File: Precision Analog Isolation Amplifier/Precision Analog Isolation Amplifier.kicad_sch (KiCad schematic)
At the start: 20 parts, among them J1 Conn_Coaxial, J2 Conn_Coaxial, Q1 2N3906, U1 HCNR201, U2 TLV172IDCK, U3 TLV172IDCK

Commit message: Add few components & Start PCB design
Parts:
- added C1, C13, C5, C9: 47u, Capacitor_SMD:C_0805_2012Metric_Pad1.18x1.45mm_HandSolder, symbol Device:C
- added C11, C12, C15, C16, C3, C4, C7, C8: C, Capacitor_SMD:C_0805_2012Metric_Pad1.18x1.45mm_HandSolder, symbol Device:C
- added FB1, FB2, FB3, FB4: FerriteBead_Small, Inductor_SMD:L_1206_3216Metric, symbol Device:FerriteBead_Small
- added J1, J2: Conn_01x03, Connector_PinHeader_2.54mm:PinHeader_1x03_P2.54mm_Vertical, symbol Connector_Generic:Conn_01x03
- C10: renamed from C4; footprint (none) -> Capacitor_SMD:C_0805_2012Metric_Pad1.18x1.45mm_HandSolder
- C14: renamed from C6; footprint (none) -> Capacitor_SMD:C_0805_2012Metric_Pad1.18x1.45mm_HandSolder
- C17: renamed from C2; footprint (none) -> Capacitor_SMD:C_0805_2012Metric_Pad1.18x1.45mm_HandSolder
- C18: renamed from C5; value C -> 33p; footprint (none) -> Capacitor_SMD:C_0805_2012Metric_Pad1.18x1.45mm_HandSolder
- C2: renamed from C1; footprint (none) -> Capacitor_SMD:C_0805_2012Metric_Pad1.18x1.45mm_HandSolder
- C6: renamed from C3; footprint (none) -> Capacitor_SMD:C_0805_2012Metric_Pad1.18x1.45mm_HandSolder
- J3: renamed from J1; footprint (none) -> Connector_Coaxial:SMA_Amphenol_132289_EdgeMount
- J4: renamed from J2; footprint (none) -> Connector_Coaxial:SMA_Amphenol_132289_EdgeMount
- R1, R2, R3, R6: footprint (none) -> Resistor_SMD:R_0805_2012Metric_Pad1.20x1.40mm_HandSolder
- R4: renamed from R5; footprint (none) -> Resistor_SMD:R_0805_2012Metric_Pad1.20x1.40mm_HandSolder
- R5: renamed from R4; footprint (none) -> Resistor_SMD:R_0805_2012Metric_Pad1.20x1.40mm_HandSolder
- RV1: footprint (none) -> Potentiometer_THT:Potentiometer_Bourns_3386W_Horizontal
- U2, U3: footprint Package_TO_SOT_SMD:SOT-353_SC-70-5 -> (none)
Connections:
- net GND1: now also C1.1, C3.1, C4.1, C5.1, C7.1, C8.1, J1.2 (Pin_2)
- net GND2: now also C11.1, C12.1, C13.1, C15.1, C16.1, C9.1, J2.2 (Pin_2)
- net VCC1 +15V: now also FB1.1, J1.1 (Pin_1); no longer C2.2
- net VCC2 +15V: now also FB3.1, J2.1 (Pin_1); no longer C10.2
- net VEE1 -15V: now also FB2.1, J1.3 (Pin_3); no longer C6.2
- net VEE2 -15V: now also FB4.1, J2.3 (Pin_3); no longer C14.2
- new net: C1.2, C2.2, C3.2, C4.2, FB1.2
- new net: C13.2, C14.2, C15.2, C16.2, FB4.2
- new net: C5.2, C6.2, C7.2, C8.2, FB2.2
- new net: C10.2, C11.2, C12.2, C9.2, FB3.2
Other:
- moved on the sheet: C10, C14, C17, C18, C2, C6, D1, J3, J4, Q1, R1, R2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

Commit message: Update Schematic & PCB
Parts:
- removed U2, U3: TLV172IDCK, symbol Amplifier_Operational:TLV172IDCK
- added C19, C20: 0.1uF, Capacitor_SMD:C_0805_2012Metric_Pad1.18x1.45mm_HandSolder, symbol Device:C
- added IC1: ADA4899-1YRDZ, SOIC127P600X175-9N, symbol ADA4899:ADA4899-1YRDZ
- added R7: 50R, Resistor_SMD:R_0805_2012Metric_Pad1.20x1.40mm_HandSolder, symbol Device:R
- added U2, U4: ADA4522, ADA4522:SOIC127P600X175-8N, symbol Amplifier_Operational:OPA1692xDGK
- D1: value 1N4150 -> ---; footprint (none) -> Diode_SMD:D_0805_2012Metric_Pad1.15x1.40mm_HandSolder
- Q1: value 2N3906 -> ---; footprint (none) -> Package_TO_SOT_SMD:SOT-23_Handsoldering
- U1: footprint (none) -> HCNR201-300E:HCNR201300E
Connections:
- net GND1: now also U4.3 (+)
- net GND2: now also C19.1, C20.1, IC1.9 (EP), U2.3 (+)
- net VCC1 +15V: now also C1.2, C2.2, C3.2, C4.2, FB1.2, U4.8 (V+); no longer FB1.1, J1.1 (Pin_1)
- net VCC2 +15V: now also C10.2, C11.2, C12.2, C9.2, FB3.2, C20.2, IC1.7 (+VS), U2.8 (V+); no longer FB3.1, J2.1 (Pin_1)
- net VEE1 -15V: now also C5.2, C6.2, C7.2, C8.2, FB2.2, U4.4 (V-); no longer FB2.1, J1.3 (Pin_3)
- net VEE2 -15V: now also C13.2, C14.2, C15.2, C16.2, FB4.2, C19.2, IC1.4 (-VS_1), U2.4 (V-); no longer FB4.1, J2.3 (Pin_3)
- net at C17.1, R4.2, U1.3 (K): now also U4.2 (-)
- net at C17.2, R3.2: now also U4.1
- net at C18.2, R6.1, U1.6 (K): now also U2.2 (-)
- net Vsep_out: now reaches C18.1, RV1.1, RV1.2
- net Vsep_out: now also R7.1, U2.1; no longer J4.1 (In)
- new net: IC1.3 (+IN), R7.2
- new net VCC1 IN +15V: FB1.1, J1.1 (Pin_1)
- new net VCC2 IN +15V: FB3.1, J2.1 (Pin_1)
- new net VEE1 IN -15V: FB2.1, J1.3 (Pin_3)
- new net VEE2 IN -15V: FB4.1, J2.3 (Pin_3)
- new net Vout: IC1.2 (-IN), IC1.6 (VOUT), J4.1 (In)
- no-connect marks 0 -> 9
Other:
- note added: "Część pierwotna"
- note added: "Część wtórna"
- note added: "NC"
- note added: "Wtórnik napięciowy"
- note added: "Zasilanie"
- moved on the sheet: C1, C10, C11, C12, C13, C14, C15, C16, C17, C18, C2, C3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

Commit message: Update PCB
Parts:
- added D2, D3, D4, D5: SMAJ15A, Diode_SMD:D_SMA, symbol Diode:SMAJ15A
- added D6, D7, D8, D9: LED, Diode_SMD:D_0805_2012Metric_Pad1.15x1.40mm_HandSolder, symbol Device:LED
- added F1, F2, F3, F4: Fuse, Resistor_SMD:R_0805_2012Metric_Pad1.20x1.40mm_HandSolder, symbol Device:Fuse
- added R10, R11, R8, R9: 33k, Resistor_SMD:R_0805_2012Metric_Pad1.20x1.40mm_HandSolder, symbol Device:R
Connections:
- net GND1: now also D2.1 (A1), D3.2 (A2), R8.2, R9.2
- net GND2: now also D4.1 (A1), D5.2 (A2), R10.2, R11.2
- net VCC1 +15V: now also D6.2 (A)
- net VCC1 IN +15V: now also D3.1 (A1), F2.1; no longer J1.1 (Pin_1)
- net VCC2 +15V: now also D9.2 (A)
- net VCC2 IN +15V: now also D5.1 (A1), F3.1; no longer J2.1 (Pin_1)
- net VEE1 -15V: now also D7.1 (K)
- net VEE1 IN -15V: now also D2.2 (A2), F1.1; no longer J1.3 (Pin_3)
- net VEE2 -15V: now also D8.1 (K)
- net VEE2 IN -15V: now also D4.2 (A2), F4.1; no longer J2.3 (Pin_3)
- new net: F3.2, J2.1 (Pin_1)
- new net: D8.2 (A), R10.1
- new net: D6.1 (K), R8.1
- new net: D9.1 (K), R11.1
- new net: F2.2, J1.1 (Pin_1)
- new net: F1.2, J1.3 (Pin_3)
- new net: D7.2 (A), R9.1
- new net: F4.2, J2.3 (Pin_3)
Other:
- moved on the sheet: J1

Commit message: Update PCB layout
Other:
- moved on the sheet: D2, D3, D4, D5, F1, F2, F3, F4, J1, J2

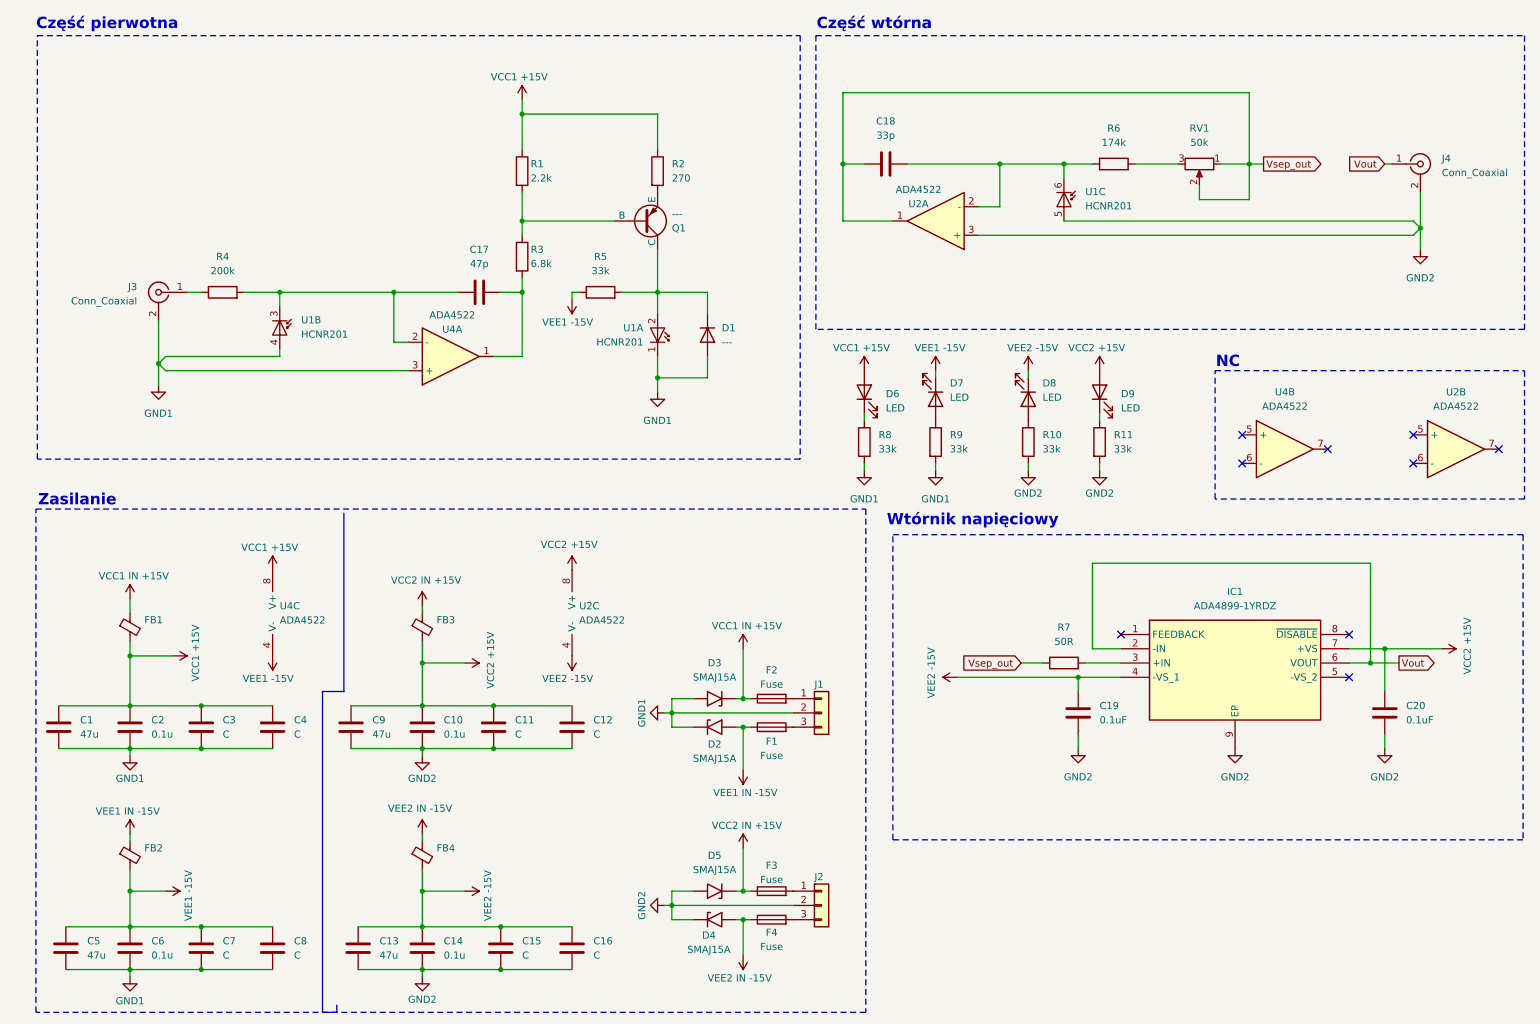
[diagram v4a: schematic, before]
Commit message: Update Schematic and Add Tracks to PCB
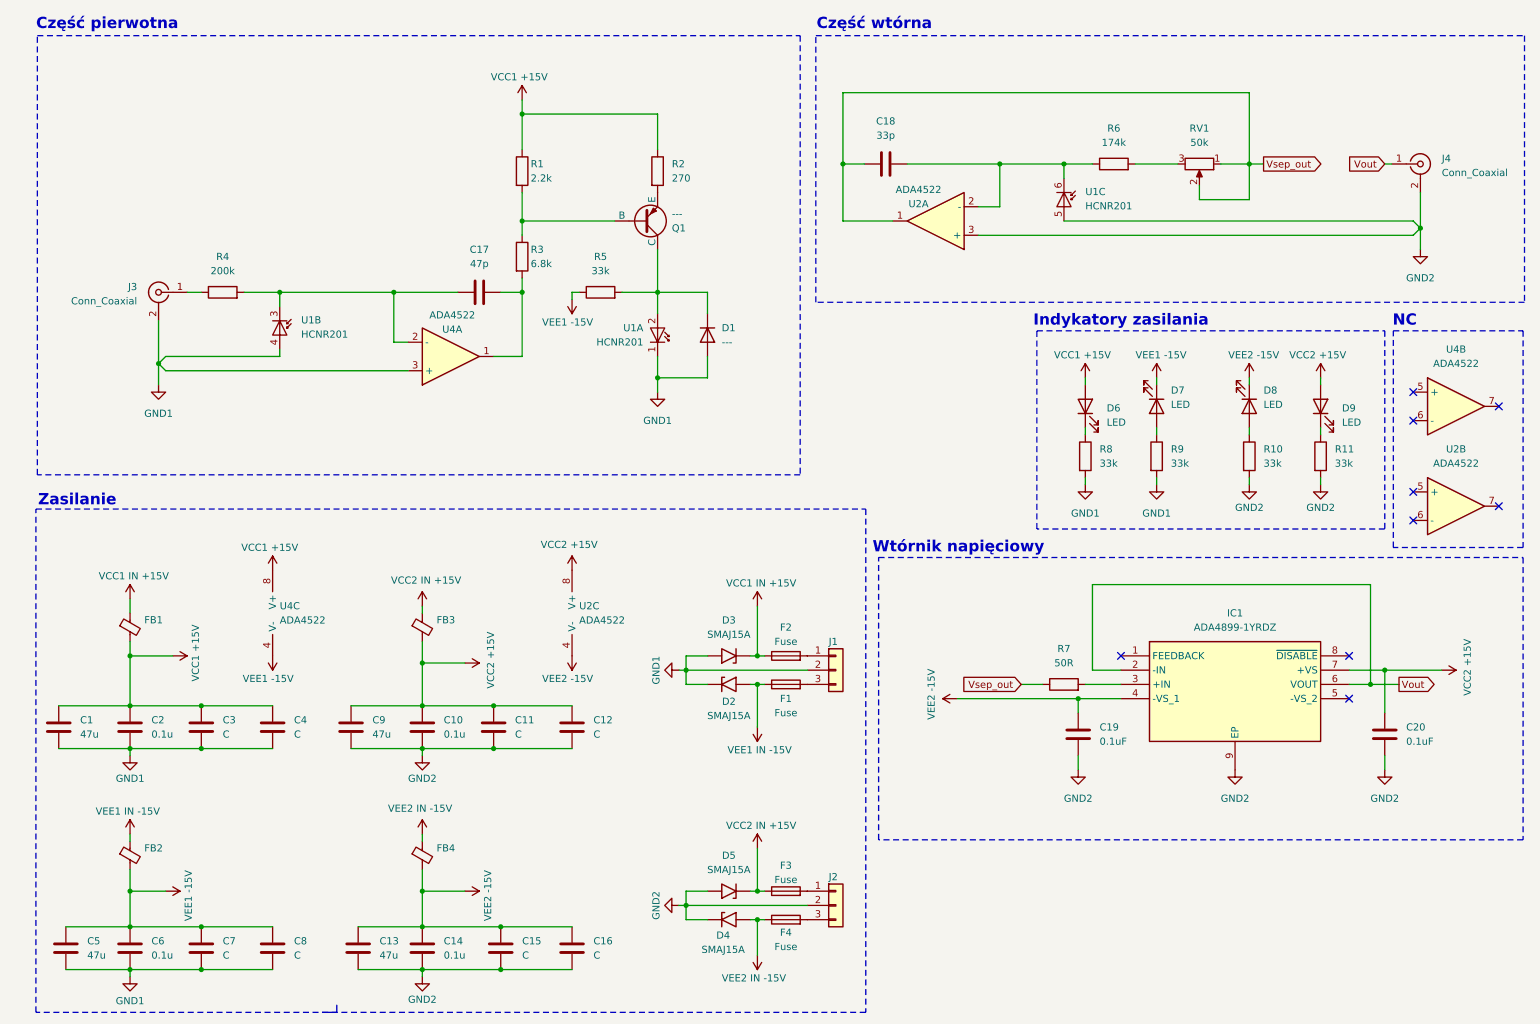
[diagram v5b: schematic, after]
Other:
- note added: "Indykatory zasilania"
- moved on the sheet: C19, C20, D2, D3, D4, D5, D6, D7, D8, D9, F1, F2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

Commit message: update pcb
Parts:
- J3, J4: footprint Connector_Coaxial:SMA_Amphenol_132289_EdgeMount -> CONN SMA JACK STR 50 OHM SMD:CONN_732511350_MOL
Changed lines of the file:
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@@
 			)
 		)
-		(property "Footprint" "Connector_Coaxial:SMA_Amphenol_132289_EdgeMount"
+		(property "Footprint" "CONN SMA JACK STR 50 OHM SMD:CONN_732511350_MOL"
 			(at 38.1 66.04 0)
 			(effects
@@
 			)
 		)
-		(property "Footprint" "Connector_Coaxial:SMA_Amphenol_132289_EdgeMount"
+		(property "Footprint" "CONN SMA JACK STR 50 OHM SMD:CONN_732511350_MOL"
 			(at 262.89 43.18 0)
 			(effects

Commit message: Update PCB & Schematic
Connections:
- net GND1: now also U4.5 (+)
- net GND2: now also U2.5 (+)
- net at U4.6 (-): now also U4.7
- net at U2.6 (-): now also U2.7
- no-connect marks 9 -> 3
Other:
- moved on the sheet: D6, D7, D8, D9, R10, R11, R8, R9, U2B, U4B
